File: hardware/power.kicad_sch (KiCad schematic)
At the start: 23 parts, among them J9 24V_Power, U1 K7805-500R3, U4 LM3671MFX-3.3/NOPB

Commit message: Refactoring
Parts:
- removed TP2: 5V_USB, TestPoint:TestPoint_Pad_D2.0mm, symbol Connector:TestPoint
- removed TP3: 5V, TestPoint:TestPoint_Pad_D2.0mm, symbol Connector:TestPoint
- removed TP4: 3.3V, TestPoint:TestPoint_Pad_D2.0mm, symbol Connector:TestPoint
- C4: renamed from C3; DIGIKEY Part # (none) -> 565-EMHB500ARA681MMH0S-ND
- C5: renamed from C4; DIGIKEY Part # (none) -> 4713-GMC31X7R475K50NTCT-ND; MP (none) -> GMC31X7R475K50NT
- C7: LCSC Part # C23733 -> C87998
- C9: renamed from C8; LCSC Part # C19702 -> C15850
- D4: renamed from D27; footprint Diode_THT:D_DO-41_SOD81_P10.16mm_Horizontal -> Diode_SMD:D_SOD-323_HandSoldering; JLCPCB Part # C3033976 -> (none); LCSC Part # C3033976 -> C191023
- J6: renamed from J9; footprint Connector_PinHeader_2.00mm:PinHeader_1x02_P2.00mm_Horizontal -> Connector_Wire:SolderWire-0.1sqmm_1x02_P3.6mm_D0.4mm_OD1mm_Relief
- R14: renamed from R42; LCSC Part # C17659 -> C17544
- R15: renamed from R44; LCSC Part # C17659 -> C17544
- RV1: LCSC Part # LCSC Part # -> C20966
- renumbered C5 to C6, C6 to C8, D25 to D3, D29 to D5, D28 to D6, U1 to U3
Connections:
- net 24V: now reaches F1.1, J6.1 (Pin_1)

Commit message: Release hardware design v1.0 for manufacturing
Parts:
- J5: renamed from J6; footprint Connector_Wire:SolderWire-0.1sqmm_1x02_P3.6mm_D0.4mm_OD1mm_Relief -> TerminalBlock_Phoenix:TerminalBlock_Phoenix_MKDS-1,5-2-5.08_1x02_P5.08mm_Horizontal; symbol Connector_Generic:Conn_01x02 -> Connector:Conn_01x02_Pin; LCSC Part # (none) -> C2915639; now fitted; now in the parts list
- renumbered C4 to C10, C8 to C11, C7 to C12, C9 to C13, C6 to C5, C5 to C9, D3 to D5, D4 to D6, D6 to D7, D5 to D8, L2 to L1, L1 to L2, R15 to R16, R14 to R17, U4 to U3, U3 to U4
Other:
- moved on the sheet: J5
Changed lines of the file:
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@@
 		(dnp no)
 		(fields_autoplaced yes)
-		(property "Reference" "C4"
+		(property "Reference" "C10"
 			(at 77.851 113.4688 0)
 			(effects
@@
 			(project "watermeter"
 				(path "/606c32de-c78d-4f57-8623-12dddfc87e44/e81e9ebb-b95f-4963-a7bf-ac73a3dd4d4b"
-					(reference "C4")
+					(reference "C10")
 					(unit 1)
 				)
@@
 		(on_board yes)
 		(dnp no)
-		(property "Reference" "D3"
+		(property "Reference" "D5"
 			(at 40.64 114.935 90)
 			(effects
@@
 			(project "watermeter"
 				(path "/606c32de-c78d-4f57-8623-12dddfc87e44/e81e9ebb-b95f-4963-a7bf-ac73a3dd4d4b"
-					(reference "D3")
+					(reference "D5")
 					(unit 1)
 				)
@@
 		(dnp no)
 		(fields_autoplaced yes)
-		(property "Reference" "R14"
+		(property "Reference" "R17"
 			(at 229.108 104.1978 0)
 			(effects
@@
 			(project "watermeter"
 				(path "/606c32de-c78d-4f57-8623-12dddfc87e44/e81e9ebb-b95f-4963-a7bf-ac73a3dd4d4b"
-					(reference "R14")
+					(reference "R17")
 					(unit 1)
 				)
@@
 	)
 	(symbol
-		(lib_id "Connector_Generic:Conn_01x02")
+		(lib_id "Connector:Conn_01x02_Pin")
 		(at 27.94 118.11 0)
-		(mirror y)
 		(unit 1)
 		(exclude_from_sim no)
-		(in_bom no)
+		(in_bom yes)
 		(on_board yes)
-		(dnp yes)
-		(property "Reference" "J6"
-			(at 28.6512 118.1678 0)
+		(dnp no)
+		(property "Reference" "J5"
+			(at 27.2288 118.1678 0)
 			(effects
 				(font
@@
 		)
 		(property "Value" "24V_Power"
-			(at 28.6512 120.5921 0)
+			(at 27.2288 120.5921 0)
 			(effects
 				(font
@@
 			)
 		)
-		(property "Footprint" "Connector_Wire:SolderWire-0.1sqmm_1x02_P3.6mm_D0.4mm_OD1mm_Relief"
+		(property "Footprint" "TerminalBlock_Phoenix:TerminalBlock_Phoenix_MKDS-1,5-2-5.08_1x02_P5.08mm_Horizontal"
 			(at 27.94 118.11 0)
 			(effects
@@
 			)
 		)
-		(property "Description" "Generic connector, single row, 01x02, script generated (kicad-library-utils/schlib/autogen/connector/)"
+		(property "Description" "Generic connector, single row, 01x02, script generated"
 			(at 27.94 118.11 0)
 			(effects
@@
 			)
 		)
+		(property "LCSC Part #" "C2915639"
+			(at 27.94 118.11 0)
+			(effects
+				(font
+					(size 1.27 1.27)
+				)
+				(hide yes)
+			)
+		)
 		(pin "1"
 		)
@@
 			(project "watermeter"
 				(path "/606c32de-c78d-4f57-8623-12dddfc87e44/e81e9ebb-b95f-4963-a7bf-ac73a3dd4d4b"
-					(reference "J6")
+					(reference "J5")
 					(unit 1)
 				)
@@
 		(dnp no)
 		(fields_autoplaced yes)
-		(property "Reference" "C7"
+		(property "Reference" "C12"
 			(at 176.911 73.7178 0)
 			(effects
@@
 			(project "watermeter"
 				(path "/606c32de-c78d-4f57-8623-12dddfc87e44/e81e9ebb-b95f-4963-a7bf-ac73a3dd4d4b"
-					(reference "C7")
+					(reference "C12")
 					(unit 1)
 				)
@@
 		(dnp no)
 		(fields_autoplaced yes)
-		(property "Reference" "C6"
+		(property "Reference" "C5"
 			(at 131.191 116.8979 0)
 			(effects
@@
 			(project "watermeter"
 				(path "/606c32de-c78d-4f57-8623-12dddfc87e44/e81e9ebb-b95f-4963-a7bf-ac73a3dd4d4b"
-					(reference "C6")
+					(reference "C5")
 					(unit 1)
 				)
@@
 		(dnp no)
 		(fields_autoplaced yes)
-		(property "Reference" "D5"
+		(property "Reference" "D8"
 			(at 229.108 96.5143 90)
 			(effects
@@
 			(project "watermeter"
 				(path "/606c32de-c78d-4f57-8623-12dddfc87e44/e81e9ebb-b95f-4963-a7bf-ac73a3dd4d4b"
-					(reference "D5")
+					(reference "D8")
 					(unit 1)
 				)
@@
 		(dnp no)
 		(fields_autoplaced yes)
-		(property "Reference" "R15"
+		(property "Reference" "R16"
 			(at 240.538 82.6078 0)
 			(effects
@@
 			(project "watermeter"
 				(path "/606c32de-c78d-4f57-8623-12dddfc87e44/e81e9ebb-b95f-4963-a7bf-ac73a3dd4d4b"
-					(reference "R15")
+					(reference "R16")
 					(unit 1)
 				)
@@
 		(dnp no)
 		(fields_autoplaced yes)
-		(property "Reference" "D6"
+		(property "Reference" "D7"
 			(at 240.538 73.6543 90)
 			(effects
@@
 			(project "watermeter"
 				(path "/606c32de-c78d-4f57-8623-12dddfc87e44/e81e9ebb-b95f-4963-a7bf-ac73a3dd4d4b"
-					(reference "D6")
+					(reference "D7")
 					(unit 1)
 				)
@@
 		(dnp no)
 		(fields_autoplaced yes)
-		(property "Reference" "C8"
+		(property "Reference" "C11"
 			(at 215.011 111.8179 0)
 			(effects
@@
 			(project "watermeter"
 				(path "/606c32de-c78d-4f57-8623-12dddfc87e44/e81e9ebb-b95f-4963-a7bf-ac73a3dd4d4b"
-					(reference "C8")
+					(reference "C11")
 					(unit 1)
 				)
@@
 		(on_board yes)
 		(dnp no)
-		(property "Reference" "L2"
+		(property "Reference" "L1"
 			(at 111.76 103.3004 90)
 			(effects
@@
 			(project "watermeter"
 				(path "/606c32de-c78d-4f57-8623-12dddfc87e44/e81e9ebb-b95f-4963-a7bf-ac73a3dd4d4b"
-					(reference "L2")
+					(reference "L1")
 					(unit 1)
 				)
@@
 		(dnp no)
 		(fields_autoplaced yes)
-		(property "Reference" "U3"
+		(property "Reference" "U4"
 			(at 179.07 102.5355 0)
 			(effects
@@
 			(project "watermeter"
 				(path "/606c32de-c78d-4f57-8623-12dddfc87e44/e81e9ebb-b95f-4963-a7bf-ac73a3dd4d4b"
-					(reference "U3")
+					(reference "U4")
 					(unit 1)
 				)
@@
 		(dnp no)
 		(fields_autoplaced yes)
-		(property "Reference" "C9"
+		(property "Reference" "C13"
 			(at 223.901 76.2578 0)
 			(effects
@@
 			(project "watermeter"
 				(path "/606c32de-c78d-4f57-8623-12dddfc87e44/e81e9ebb-b95f-4963-a7bf-ac73a3dd4d4b"
-					(reference "C9")
+					(reference "C13")
 					(unit 1)
 				)
@@
 		(on_board yes)
 		(dnp no)
-		(property "Reference" "C5"
+		(property "Reference" "C9"
 			(at 101.981 116.8979 0)
 			(effects
@@
 			(project "watermeter"
 				(path "/606c32de-c78d-4f57-8623-12dddfc87e44/e81e9ebb-b95f-4963-a7bf-ac73a3dd4d4b"
-					(reference "C5")
+					(reference "C9")
 					(unit 1)
 				)
@@
 		(dnp no)
 		(fields_autoplaced yes)
-		(property "Reference" "D4"
+		(property "Reference" "D6"
 			(at 161.6075 65.7057 0)
 			(effects
@@
 			(project "watermeter"
 				(path "/606c32de-c78d-4f57-8623-12dddfc87e44/e81e9ebb-b95f-4963-a7bf-ac73a3dd4d4b"
-					(reference "D4")
+					(reference "D6")
 					(unit 1)
 				)
@@
 		(dnp no)
 		(fields_autoplaced yes)
-		(property "Reference" "L1"
+		(property "Reference" "L2"
 			(at 60.96 103.3004 90)
 			(effects
@@
 			(project "watermeter"
 				(path "/606c32de-c78d-4f57-8623-12dddfc87e44/e81e9ebb-b95f-4963-a7bf-ac73a3dd4d4b"
-					(reference "L1")
+					(reference "L2")
 					(unit 1)
 				)
@@
 		(dnp no)
 		(fields_autoplaced yes)
-		(property "Reference" "U4"
+		(property "Reference" "U3"
 			(at 195.58 65.7057 0)
 			(effects
@@
 			(project "watermeter"
 				(path "/606c32de-c78d-4f57-8623-12dddfc87e44/e81e9ebb-b95f-4963-a7bf-ac73a3dd4d4b"
-					(reference "U4")
+					(reference "U3")
 					(unit 1)
 				)

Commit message: fix: unstable power supply
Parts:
- C12: value 4.7uF/10V -> 10uF/10V; footprint PCM_Capacitor_SMD_AKL:C_0805_2012Metric -> Capacitor_SMD:C_1206_3216Metric; LCSC Part # C87998 -> C577214
- C13: value 10uF -> 10uF/10V; footprint PCM_Capacitor_SMD_AKL:C_0805_2012Metric -> Capacitor_SMD:C_1206_3216Metric
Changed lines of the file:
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@@
 			)
 		)
-		(property "Value" "4.7uF/10V"
+		(property "Value" "10uF/10V"
 			(at 176.911 76.1421 0)
 			(effects
@@
 			)
 		)
-		(property "Footprint" "PCM_Capacitor_SMD_AKL:C_0805_2012Metric"
+		(property "Footprint" "Capacitor_SMD:C_1206_3216Metric"
 			(at 174.9552 78.74 0)
 			(effects
@@
 			)
 		)
-		(property "LCSC Part #" "C87998"
+		(property "LCSC Part #" "C577214"
 			(at 173.99 74.93 0)
 			(effects
@@
 			)
 		)
-		(property "Value" "10uF"
+		(property "Value" "10uF/10V"
 			(at 223.901 78.6821 0)
 			(effects
@@
 			)
 		)
-		(property "Footprint" "PCM_Capacitor_SMD_AKL:C_0805_2012Metric"
+		(property "Footprint" "Capacitor_SMD:C_1206_3216Metric"
 			(at 221.9452 81.28 0)
 			(effects

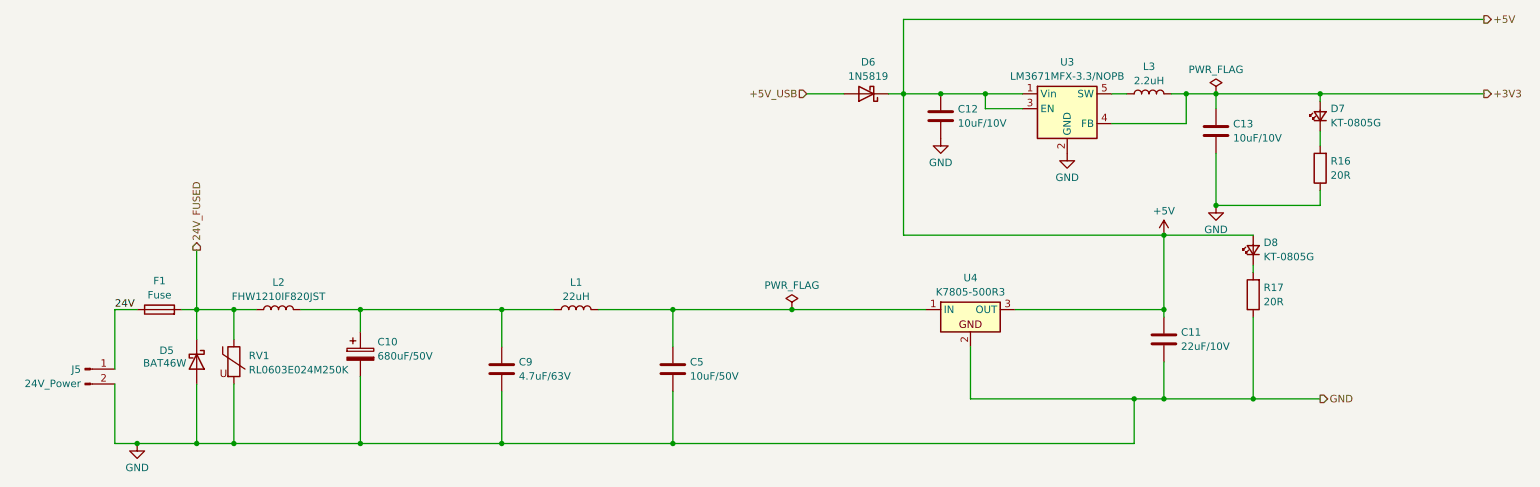
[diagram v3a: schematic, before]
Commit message: Board V2. fix: power supply fix: NTC noise suppression fix: Q1 and Q2 wrong pin numbers fix: Increased power trice width
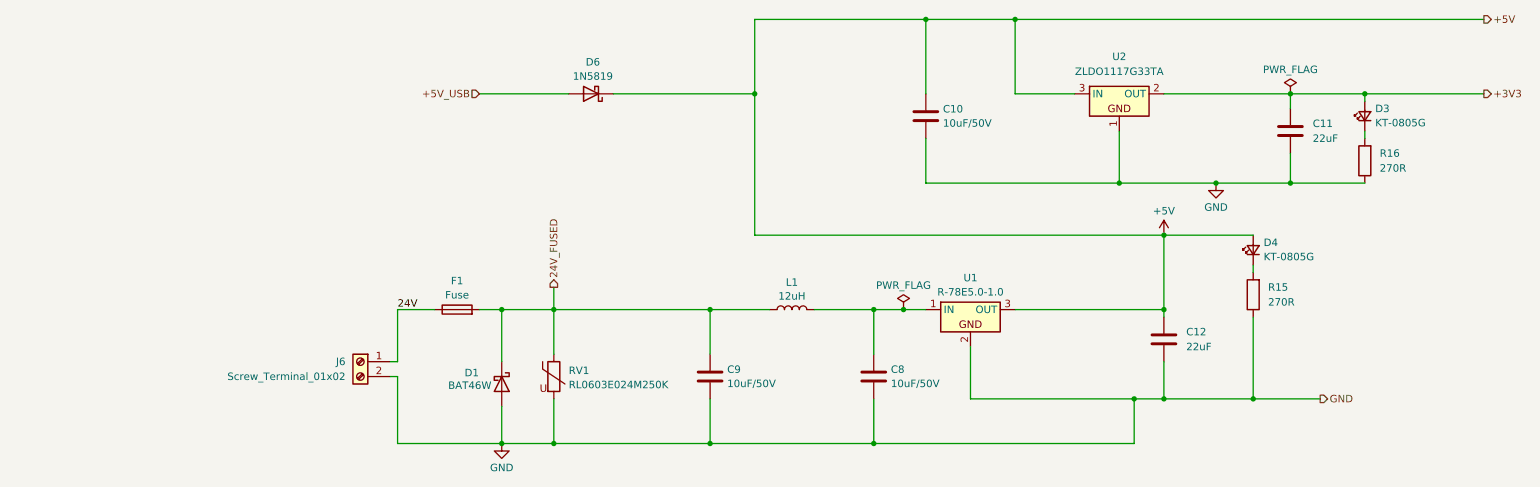
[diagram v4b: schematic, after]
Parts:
- removed C10: 680uF/50V, MyFootprints:CAP-SMD_BD12.5-L13.0-W13.0-LS14.4-FD, symbol Device:C_Polarized
- removed C12, C13: 10uF/10V, Capacitor_SMD:C_1206_3216Metric, symbol PCM_Capacitor_AKL:C_0805
- removed C5: 10uF/50V, Capacitor_SMD:C_1206_3216Metric, symbol Device:C
- removed J5: 24V_Power, TerminalBlock_Phoenix:TerminalBlock_Phoenix_MKDS-1,5-2-5.08_1x02_P5.08mm_Horizontal, symbol Connector:Conn_01x02_Pin
- removed L2: FHW1210IF820JST, Inductor_SMD:L_1210_3225Metric, symbol Device:L
- removed L3: 2.2uH, Inductor_SMD:L_1206_3216Metric, symbol Device:L
- removed U3: LM3671MFX-3.3/NOPB, Package_TO_SOT_SMD:TSOT-23-5, symbol Regulator_Switching:LM3670MF
- added C10, C8: 10uF/50V, Capacitor_SMD:C_1206_3216Metric, symbol Device:C
- added C12: 22uF, Capacitor_SMD:C_1206_3216Metric, symbol Device:C
- added J6: Screw_Terminal_01x02, TerminalBlock_Phoenix:TerminalBlock_Phoenix_MKDS-1,5-2-5.08_1x02_P5.08mm_Horizontal, symbol Connector:Screw_Terminal_01x02
- added U2: ZLDO1117G33TA, Package_TO_SOT_SMD:SOT-223-3_TabPin2, symbol PCM_Voltage_Regulator_AKL:ZLDO1117G33TA
- C11: value 22uF/10V -> 22uF; LCSC Part # C5672 -> C12891
- C9: value 4.7uF/63V -> 10uF/50V; LCSC Part # C29823 -> C13585
- L1: value 22uH -> 12uH; footprint Inductor_SMD:L_0603_1608Metric -> MyFootprints:IND_ASPI-6045S-120M-T; LCSC Part # C6808015 -> C168077
- R15: renamed from R17; value 20R -> 270R; footprint Resistor_SMD:R_0805_2012Metric -> Digikey library:LED_0603; LCSC Part # C17544 -> C22966
- R16: value 20R -> 270R; footprint Resistor_SMD:R_0805_2012Metric -> Digikey library:LED_0603; LCSC Part # C17544 -> C22966
- U1: renamed from U4; value K7805-500R3 -> R-78E5.0-1.0; LCSC Part # C909662 -> C22371890
- renumbered D5 to D1, D7 to D3, D8 to D4
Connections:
- net +3V3: now also C11.1, U2.2 (OUT)
- net +5V: now also C10.1, C12.1, U2.3 (IN); no longer C11.1
- net 24V: now also J6.1 (Pin_1)
- net 24V_FUSED: now also C9.1, L1.1
- net GND: now also C10.2, C12.2, C8.2, J6.2 (Pin_2), U2.1
- net at L1.2, U1.1 (IN): now also C8.1
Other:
- moved on the sheet: D1, D3, D6, F1, L1, R16, RV1
